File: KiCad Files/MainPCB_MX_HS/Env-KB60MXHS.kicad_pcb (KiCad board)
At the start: 2 copper layers, 283 x 126.5 mm, 153 parts, among them J1 Conn_01x04, SW1 EVQ-P7A01P, U1 Pico

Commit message: fixed alignment issues, generated gerbers, fixed silkscreen issues, fixed footprints, generated gerbers
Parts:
- H1, H10, H11, H2, H3, H4, H6, H9: value SMTSO2020CTJ -> SMTSO2035CTJ
- K_1, K_10, K_11, K_12, K_13, K_14, K_15, K_16, K_17, K_18, K_19, K_2, K_20, K_21, K_22, K_23, K_24, K_25, K_26, K_27, K_28, K_29, K_3, K_30, K_31, K_32, K_33, K_34, K_35, K_36, K_37, K_38, K_39, K_4, K_40, K_41, K_42, K_43, K_44, K_45, K_46, K_47, K_48, K_49, K_5, K_50, K_51, K_52, K_53, K_54, K_55, K_56, K_57, K_58, K_59, K_6, K_60, K_61, K_62, K_63, K_64, K_65, K_7, K_8, K_9: footprint MX_Only:MXOnly-1U-Hotswap-Modified -> Env_Extras:MXOnly-1U-Hotswap-Modified
- moved H9 0.77 mm to (218.9, 84.7)
- moved H4 0.70 mm to (102.2, 84.7)
- moved H10 0.57 mm to (314.1, 84.7)
- moved H1 0.08 mm to (233.2, 122.8)
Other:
- board text added: "EnvKB-60F Rev-2.1"
- board text added: "LIL DELIRIUM"
- board text added: "Soldering these pads are required for USB to work"
- board text added: "This space bar doesnt stock milk."
- board text added: "https://github.com/Envious-Data/Env-KB60F Version: 2.1"
- board text removed: "EnvKB-60F Rev-2.0"
- board text removed: "https://github.com/Envious-Data/Env-KB60F Version: 2.0"

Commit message: updated BOM,CPL to include missing parts needed, updated the values
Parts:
- D_1, D_10, D_11, D_12, D_13, D_14, D_15, D_16, D_17, D_18, D_19, D_2, D_20, D_21, D_22, D_23, D_24, D_25, D_26, D_27, D_28, D_29, D_3, D_30, D_31, D_32, D_33, D_34, D_35, D_36, D_37, D_38, D_39, D_4, D_40, D_41, D_42, D_43, D_44, D_45, D_46, D_47, D_48, D_49, D_5, D_50, D_51, D_52, D_53, D_54, D_55, D_56, D_57, D_58, D_59, D_590, D_591, D_6, D_60, D_61, D_62, D_63, D_7, D_8, D_9: value 1n4148W -> LL4148
- D_64: value 1n4007 SOD-123 -> 1n5817W
- K_1, K_10, K_11, K_12, K_13, K_14, K_15, K_16, K_17, K_18, K_19, K_2, K_20, K_21, K_22, K_23, K_24, K_25, K_26, K_27, K_28, K_29, K_3, K_30, K_31, K_32, K_33, K_34, K_35, K_36, K_37, K_38, K_39, K_4, K_40, K_41, K_42, K_43, K_44, K_45, K_46, K_47, K_48, K_49, K_5, K_50, K_51, K_52, K_53, K_54, K_55, K_56, K_57, K_58, K_59, K_6, K_60, K_61, K_62, K_63, K_64, K_65, K_7, K_8, K_9: value KEYSW -> CPG151101S11
- SW1: value EVQ-P7A01P -> EVQPUL; footprint PanasonicEVQ-P7A01P:Panasonic-EVQ-P7A01P-0-0-MFG -> Button_Switch_SMD:Panasonic_EVQPUL_EVQPUC
- USB1: value HRO-TYPE-C-31-M-14 -> TYPE-C-31-M-14
- moved SW1 0.70 mm to (358.0, 74.5), turned to -90 degrees
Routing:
- net RUNPIN: track 35.2 -> 42.3 mm

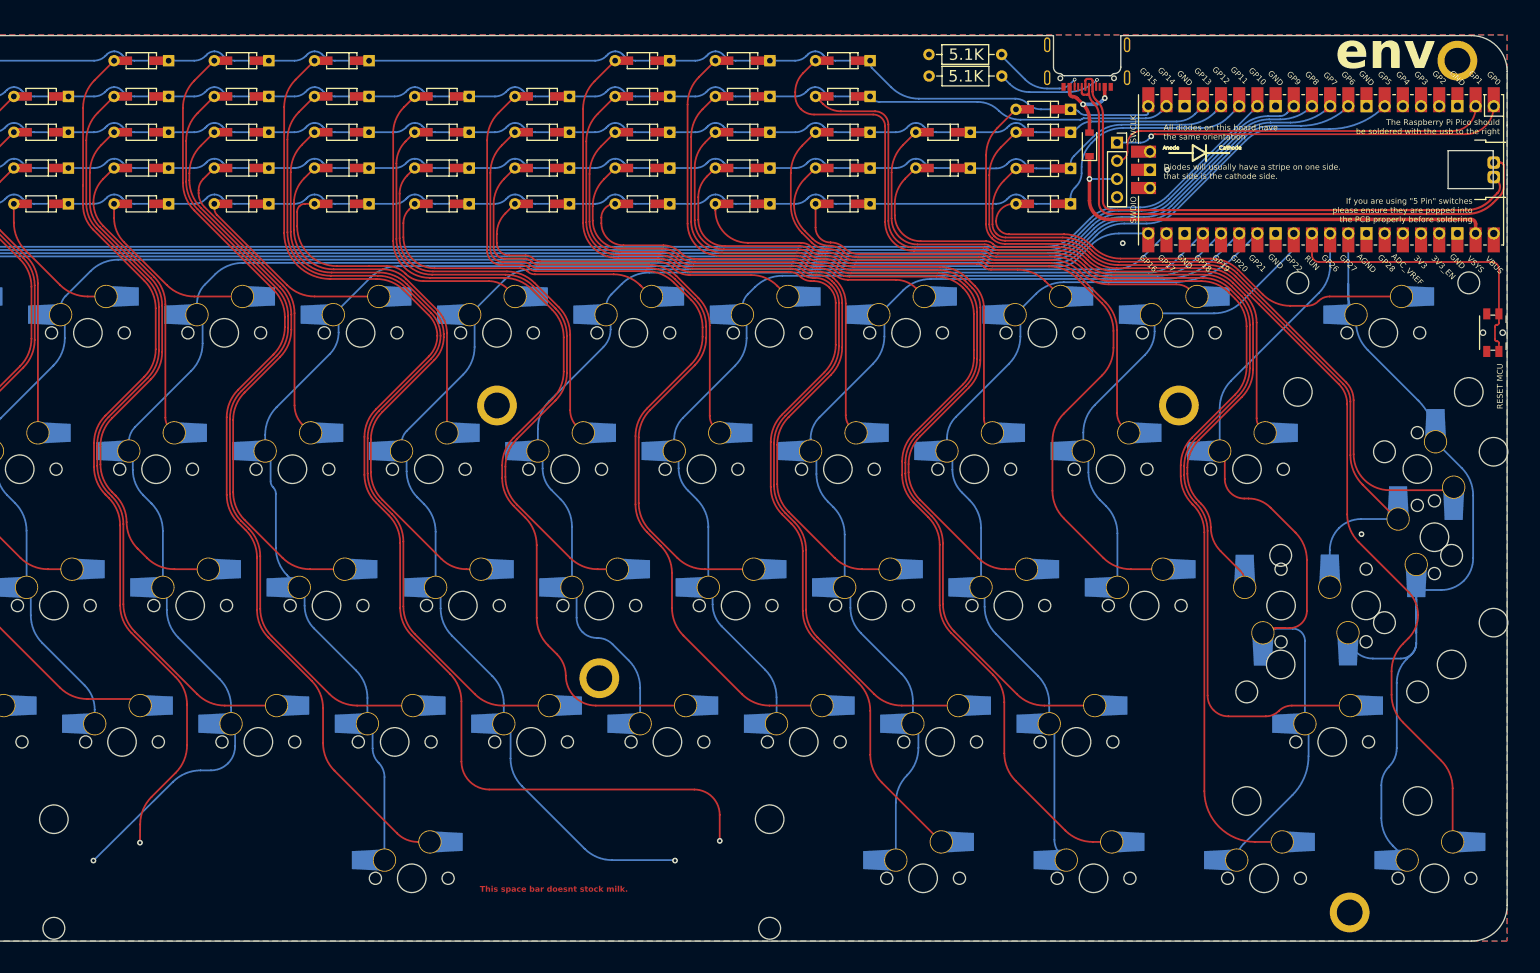
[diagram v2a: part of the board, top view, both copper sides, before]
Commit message: Corrected Several issues pointed out by Dasky (tyvm), reduced top cover size to not conflict with the plate, swapped oled header power for correct voltage, extended several pads to make it easier to hand solder, extended stabiliser slots to make board outline less sharp,
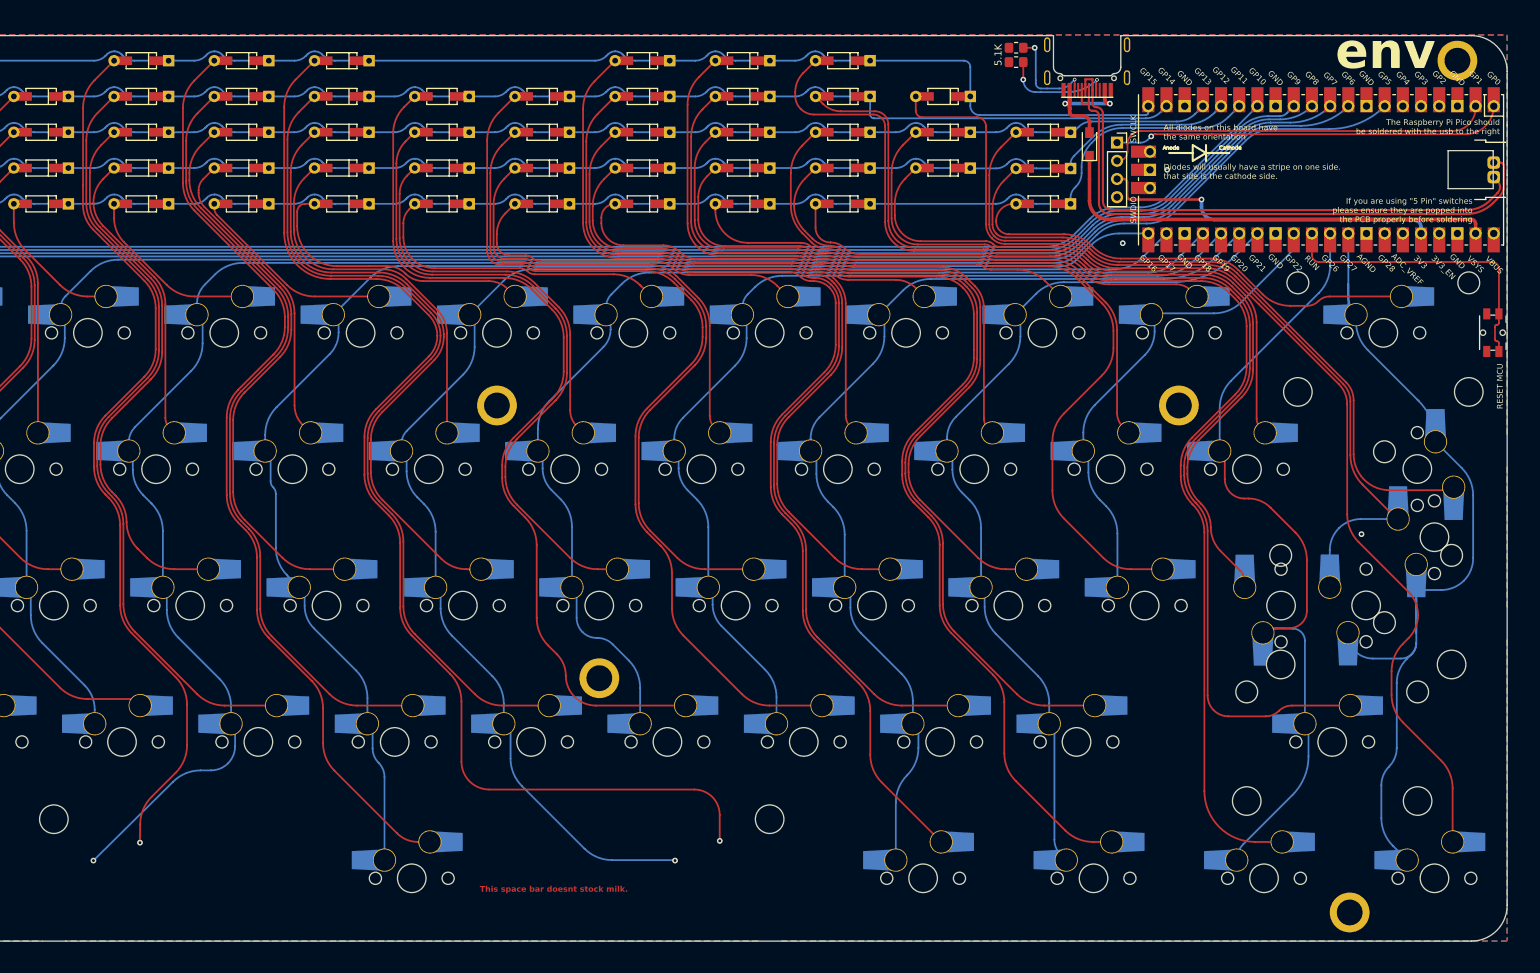
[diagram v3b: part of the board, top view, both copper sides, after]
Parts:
- 5.1K1, 5.1K2: value 5.1K 0402 Resistor -> 5.1K 0805 Resistor; footprint Resistor_THT:R_Axial_DIN0207_L6.3mm_D2.5mm_P10.16mm_Horizontal -> Resistor_SMD:R_0805_2012Metric_Pad1.20x1.40mm_HandSolder
- moved D_63 14.1 mm to (285.0, 41.5)
- moved 5.1K2 12.2 mm to (291.4, 34.7)
- moved 5.1K1 2.79 mm to (291.4, 36.7)
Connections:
- J1 pad 3: VSYS -> Net-(J1-Pin_3)
- U1 pad 36: unconnected-(U1-3V3-Pad36) -> Net-(J1-Pin_3)
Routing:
- net Net-(J1-Pin_3): track 0.00 -> 48.3 mm, vias 0 -> 1
- net Net-(D_63-A): track 147.6 -> 156.7 mm
- net VBUS: track 12.5 -> 20.6 mm
- net row4: track 215.1 -> 219.9 mm
- net VSYS: track 67.2 -> 63.3 mm, vias 1 -> 0
- net row3: track 218.5 -> 220.9 mm
- net USB2_P: track 82.4 -> 83.7 mm
- net USB2_N: track 77.8 -> 78.7 mm
- net Net-(USB1-CC2): track 13.1 -> 13.9 mm, vias 1 -> 2
- net Net-(USB1-CC1): track 15.5 -> 15.1 mm, vias 1 -> 2
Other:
- board text added: "Parts Needed: 70x 1n4148 Diodes 2x 5.1K 0805 resistors 70x switches 7x 2u MX stabilizers (or 1x6.25u + 4x 2u stabs) 1x Raspberry Pi Pico 2x 1x20 Male and/or female headers 10x M2 mounting hardware. 1x Type-C-31-M-14"
- board text removed: "Parts Needed: 70x 1n4148 Diodes 2x 5.1K 1/4W resistors 70x switches 7x 2u MX stabilizers (or 1x6.25u + 4x 2u stabs) 1x Raspberry Pi Pico 2x 1x20 Male and/or female headers 10x M2 mounting hardware. 1x Type-C-31-M-14"
